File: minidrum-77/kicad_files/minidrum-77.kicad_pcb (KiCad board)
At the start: 2 copper layers, 20 parts, among them J1 AudioJack2_Ground, J2 AudioJack2_Ground

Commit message: First revision of DR-77/78 PCB
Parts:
- J1: value AudioJack2_Ground -> TRIG_IN; footprint MusicThingModular:NV-PJ3410_SOCKET_MONO -> kicadlib:PJ301BM; moved to B.Cu
- J2: value AudioJack2_Ground -> AUDIO_OUT; footprint MusicThingModular:NV-PJ3410_SOCKET_MONO -> kicadlib:PJ301BM; moved to B.Cu
- JP1: moved to B.Cu
- R1, R2, R3, R4, R5: footprint MusicThingModular:10MM_RESISTOR -> Resistor_THT:R_Axial_DIN0207_L6.3mm_D2.5mm_P10.16mm_Horizontal
- moved C1 85.4 mm to (143.5, 50.8), turned to 180 degrees
- moved C2 81.1 mm to (143.5, 54.6), turned to 180 degrees
- moved R1 71.6 mm to (146.1, 47.0), turned to 180 degrees
- moved D1 65.8 mm to (158.8, 61.0), turned to 180 degrees
- moved JP1 57.5 mm to (142.2, 105.4), turned to 270 degrees
- moved R4 53.8 mm to (151.1, 77.5), turned to 270 degrees
- moved J1 49.7 mm to (132.1, 45.7), turned to 180 degrees
- moved R3 45.4 mm to (151.1, 74.9), turned to 90 degrees
- moved J2 43.1 mm to (148.6, 57.1)
- moved C8 38.0 mm to (158.8, 73.7), turned to 270 degrees
- moved L1 28.9 mm to (127.0, 104.1), turned to 90 degrees
- moved C3 23.5 mm to (151.1, 96.5), turned to 90 degrees
- moved C7 23.0 mm to (158.8, 100.3), turned to 270 degrees
- moved C4 21.1 mm to (151.1, 105.4), turned to 90 degrees
- moved C9 20.4 mm to (158.8, 96.5), turned to 90 degrees
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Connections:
- JP1 pad 3: Net-(JP1-Pad3) -> (no net)
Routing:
- net Net-(C10-Pad1): track 0.00 -> 45.4 mm
- net Net-(C7-Pad1): track 0.00 -> 30.9 mm
- net Net-(C3-Pad1): track 0.00 -> 28.3 mm
- net Net-(C4-Pad1): track 0.00 -> 26.8 mm
- net Net-(JP1-Pad1): track 0.00 -> 22.6 mm
- net Net-(D1-Pad1): track 0.00 -> 20.9 mm
- net Net-(C1-Pad1): track 0.00 -> 18.9 mm
- net Net-(C1-Pad2): track 0.00 -> 12.9 mm
- added copper zone on B.Cu, net GND
- added copper zone on F.Cu, net GND
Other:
- board outline added: 41.9 x 64.8 mm

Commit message: Polish up the DR-77/78 schematic
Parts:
- added L2: , Inductor_THT:L_Radial_D10.0mm_P5.00mm_Fastron_07P, F.Cu at (153.7, 108.0)
- added SW1: ALT_COIL, Connector_PinHeader_2.54mm:PinHeader_1x03_P2.54mm_Vertical, F.Cu at (142.2, 109.2)
- C1, C10, C2, C3, C4, C5, C6, C7, C8, C9: value C -> (none)
- D1: value D -> (none)
- JP1: value ALT_COIL -> DARK_POT; footprint Connector_PinHeader_2.54mm:PinHeader_1x03_P2.54mm_Vertical -> Connector_PinHeader_2.54mm:PinHeader_1x02_P2.54mm_Vertical; moved to F.Cu
- L1: value L -> (none)
- R1, R2, R3, R4, R5: value R -> (none)
- moved C6 33.4 mm to (121.9, 110.5), turned to 0 degrees
- moved C4 24.2 mm to (127.0, 106.7), turned to 180 degrees
- moved JP1 8.52 mm to (134.6, 109.2)
- moved C3 5.08 mm to (151.1, 91.4), turned to 270 degrees
- moved C5 5.08 mm to (154.9, 91.4), turned to 270 degrees
- moved C7 1.27 mm to (157.5, 100.3), turned to 180 degrees
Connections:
- JP1 pad 2: Net-(C4-Pad1) -> GND
- L1 pad 1: Net-(JP1-Pad1) -> Net-(C4-Pad1)
- L1 pad 2: GND -> Net-(L1-Pad2)
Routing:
- net Net-(C4-Pad1): track 26.8 -> 68.3 mm
- net Net-(L1-Pad2): track 0.00 -> 31.5 mm
- net Net-(C3-Pad1): track 28.3 -> 57.1 mm
- net Net-(L2-Pad2): track 0.00 -> 12.9 mm
- net Net-(JP1-Pad1): track 22.6 -> 13.0 mm
- net Net-(C7-Pad1): track 30.9 -> 31.4 mm
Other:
- board size 41.9 x 64.8 mm -> 41.9 x 69.8 mm

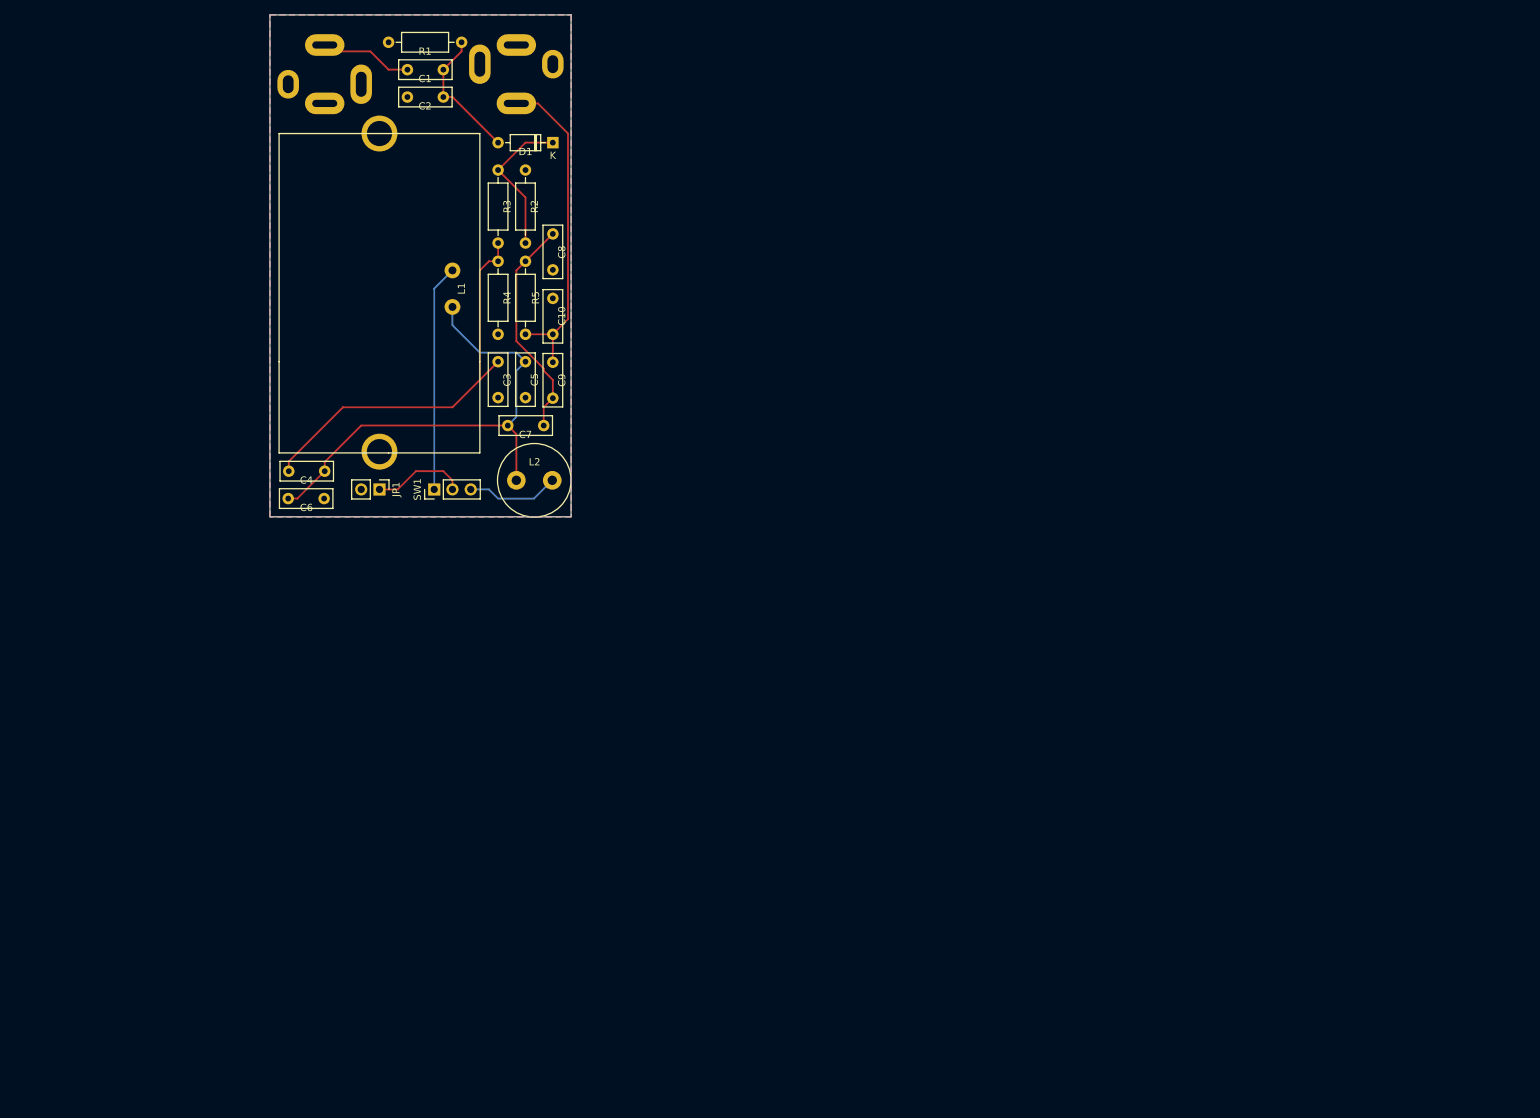
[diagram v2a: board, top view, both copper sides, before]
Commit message: Clean up, and finish PCB
Removing the worst of the switch excesses (or adding a few switches,
depending on what was in the last commit).
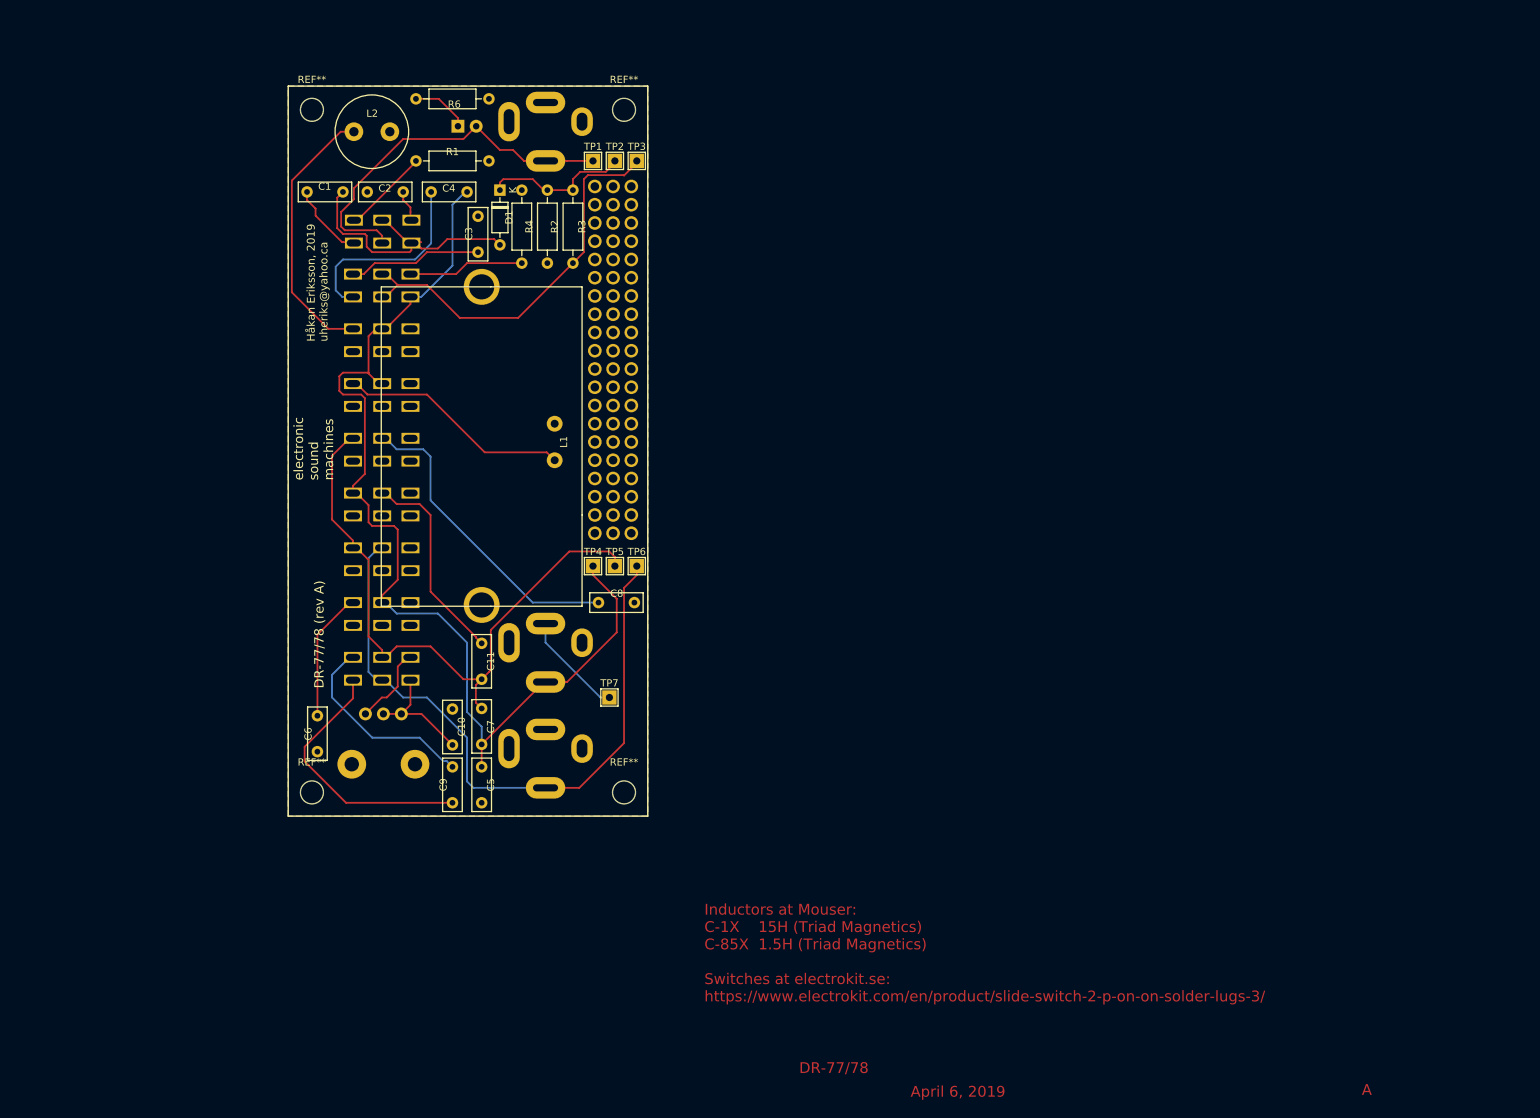
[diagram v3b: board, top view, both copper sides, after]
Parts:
- removed JP1: DARK_POT, Connector_PinHeader_2.54mm:PinHeader_1x02_P2.54mm_Vertical
- added C11: , Capacitor_THT:C_Rect_L7.2mm_W2.5mm_P5.00mm_FKS2_FKP2_MKS2_MKP2, F.Cu at (148.8, 135.6)
- added D2: LED_ALT, LED_THT:LED_D3.0mm, B.Cu at (145.5, 58.7)
- added J3: EXT_COIL, kicadlib:PJ301BM, B.Cu at (152.7, 137.7)
- added R6: , Resistor_THT:R_Axial_DIN0207_L6.3mm_D2.5mm_P10.16mm_Horizontal, F.Cu at (139.7, 54.9)
- added REF**: , kicadlib:mod_area_10x03, F.Cu at (164.6, 92.5)
- added REF**: , MountingHole:MountingHole_3.2mm_M3, F.Cu at (125.2, 56.4)
- added REF**: , MountingHole:MountingHole_3.2mm_M3, F.Cu at (168.7, 56.4)
- added REF**: , MountingHole:MountingHole_3.2mm_M3, F.Cu at (168.7, 151.4)
- added REF**: , kicadlib:mod_area_10x03, F.Cu at (164.6, 67.1)
- added REF**: , MountingHole:MountingHole_3.2mm_M3, F.Cu at (125.2, 151.4)
- added SW2: RS/C, kicadlib:DPDT_PUSH_SW, B.Cu at (123.4, 77.2)
- added SW3: C6_SEL, kicadlib:DPDT_AS_SPST_PUSH_SW, B.Cu at (123.4, 122.9)
- added SW4: COIL_1, kicadlib:DPDT_AS_SPST_PUSH_SW, B.Cu at (123.4, 92.5)
- added SW5: COIL_2, kicadlib:DPDT_AS_SPST_PUSH_SW, B.Cu at (123.4, 84.8)
- added SW6: C11_SEL, kicadlib:DPDT_AS_SPST_PUSH_SW, B.Cu at (123.4, 107.7)
- added SW7: C8_SEL, kicadlib:DPDT_AS_SPST_PUSH_SW, B.Cu at (123.4, 100.1)
- added SW8: STR_OUT, kicadlib:DPDT_AS_SPST_PUSH_SW, B.Cu at (123.4, 115.3)
- added SW9: LPF/HPF_OUT, kicadlib:DPDT_PUSH_SW, B.Cu at (123.4, 130.6)
- added TP1: , TestPoint:TestPoint_THTPad_2.0x2.0mm_Drill1.0mm, F.Cu at (164.3, 63.5)
- added TP2: , TestPoint:TestPoint_THTPad_2.0x2.0mm_Drill1.0mm, F.Cu at (167.4, 63.5)
- added TP3: , TestPoint:TestPoint_THTPad_2.0x2.0mm_Drill1.0mm, F.Cu at (170.4, 63.5)
- added TP4: , TestPoint:TestPoint_THTPad_2.0x2.0mm_Drill1.0mm, F.Cu at (164.3, 119.9)
- added TP5: , TestPoint:TestPoint_THTPad_2.0x2.0mm_Drill1.0mm, F.Cu at (167.4, 119.9)
- added TP6: , TestPoint:TestPoint_THTPad_2.0x2.0mm_Drill1.0mm, F.Cu at (170.4, 119.9)
- added TP7: DEFAULT_EXT_COIL, TestPoint:TestPoint_THTPad_2.0x2.0mm_Drill1.0mm, F.Cu at (166.6, 138.2)
- R5: value (none) -> CUTOFF; footprint Resistor_THT:R_Axial_DIN0207_L6.3mm_D2.5mm_P10.16mm_Horizontal -> Potentiometer_THT:Potentiometer_Alps_RK09K_Single_Vertical; moved to B.Cu
- SW1: value ALT_COIL -> LPF/HPF_IN; footprint Connector_PinHeader_2.54mm:PinHeader_1x03_P2.54mm_Vertical -> kicadlib:DPDT_PUSH_SW; moved to B.Cu
- moved J2 95.3 mm to (152.7, 152.4)
- moved C10 58.8 mm to (144.8, 144.8)
- moved C5 56.7 mm to (148.8, 147.8)
- moved R5 55.6 mm to (137.7, 140.5), turned to 270 degrees
- moved L2 53.5 mm to (131.1, 59.4)
- moved C9 53.2 mm to (144.8, 147.8), turned to 270 degrees
- moved C8 51.7 mm to (165.1, 125.0), turned to 0 degrees
- moved C4 43.6 mm to (146.8, 67.8)
- moved C7 40.3 mm to (148.8, 139.7), turned to 270 degrees
- moved SW1 32.5 mm to (146.6, 77.0)
- moved C6 30.5 mm to (126.0, 140.7), turned to 270 degrees
- moved J1 28.3 mm to (152.7, 65.2), turned to 0 degrees
- moved L1 25.6 mm to (141.2, 125.5)
- moved C1 22.0 mm to (129.5, 67.8)
- moved R1 17.7 mm to (139.7, 63.5), turned to 0 degrees
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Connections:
- C2 pad 1: Net-(C1-Pad1) -> Net-(C2-Pad1)
- C4 pad 2: Net-(C3-Pad1) -> Net-(C4-Pad2)
- C6 pad 1: Net-(C4-Pad1) -> Net-(C6-Pad1)
- C7 pad 1: Net-(C7-Pad1) -> Net-(C11-Pad1)
- C8 pad 1: Net-(C7-Pad1) -> Net-(C8-Pad1)
- C9 pad 1: Net-(C7-Pad1) -> Net-(C9-Pad1)
- C9 pad 2: Net-(C10-Pad1) -> Net-(C9-Pad2)
- J1 pad 3: Net-(C1-Pad2) -> Net-(D2-Pad2)
- J2 pad 3: Net-(C10-Pad1) -> Net-(J2-Pad3)
- L1 pad 1: Net-(C4-Pad1) -> Net-(L1-Pad1)
- L1 pad 2: Net-(L1-Pad2) -> GND
- L2 pad 1: Net-(C4-Pad1) -> Net-(L2-Pad1)
- L2 pad 2: Net-(L2-Pad2) -> GND
- R1 pad 1: Net-(C1-Pad1) -> Net-(R1-Pad1)
- R3 pad 1: Net-(C3-Pad1) -> Net-(R3-Pad1)
- R4 pad 1: Net-(C3-Pad1) -> Net-(R4-Pad1)
- R5 pad 2: Net-(C7-Pad1) -> Net-(C10-Pad1)
- SW1 pad 1: Net-(L1-Pad2) -> Net-(C1-Pad1)
- SW1 pad 2: Net-(JP1-Pad1) -> Net-(D2-Pad2)
- SW1 pad 3: Net-(L2-Pad2) -> Net-(C1-Pad2)
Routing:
- net Net-(J2-Pad3): track 0.00 -> 92.1 mm
- net Net-(C11-Pad1): track 0.00 -> 87.1 mm
- net Net-(C4-Pad1): track 68.3 -> 148.4 mm
- net Net-(R3-Pad1): track 0.00 -> 56.0 mm
- net Net-(D2-Pad2): track 0.00 -> 53.2 mm
- net Net-(C8-Pad1): track 0.00 -> 43.1 mm
- net Net-(C3-Pad1): track 57.1 -> 18.7 mm
- net Net-(L2-Pad1): track 0.00 -> 37.6 mm
- net Net-(C9-Pad2): track 0.00 -> 37.1 mm
- net Net-(L1-Pad1): track 0.00 -> 32.5 mm
- net Net-(L1-Pad2): track 31.5 -> 0.00 mm
- net Net-(C7-Pad1): track 31.4 -> 0.00 mm
- net Net-(C10-Pad1): track 45.4 -> 16.6 mm
- net Net-(C11-Pad2): track 0.00 -> 28.8 mm
- net Net-(C4-Pad2): track 0.00 -> 28.1 mm
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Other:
- board outline removed
- board text added: "A"
- board text added: "April 6, 2019"
- board text added: "DR-77/78"
- board text added: "DR-77/78 (rev A)"
- board text added: "Håkan Eriksson, 2019 uheriks@yahoo.ca"
- board text added: "Inductors at Mouser: C-1X 15H (Triad Magnetics) C-85X 1.5H (Triad Magnetics) Switches at electrokit.se: https://www.electrokit.com/en/product/slide-switch-2-p-on-on-solder-lugs-3/"
- board text added: "electronic sound machines"

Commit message: dr-77/78: Add logo
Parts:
- added G***: LOGO, kicadlib:esm_logo_26x13mm, F.Cu at (158.8, 112.8)
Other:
- board outline added: 50 x 101.6 mm
